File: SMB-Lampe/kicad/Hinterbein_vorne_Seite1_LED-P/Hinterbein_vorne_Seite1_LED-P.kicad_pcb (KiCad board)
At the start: 2 copper layers, 10.7 x 29.2 mm, 8 parts, among them J1 Conn_01x01_Pin, J2 Conn_01x01_Pin, J3 Conn_01x01_Pin

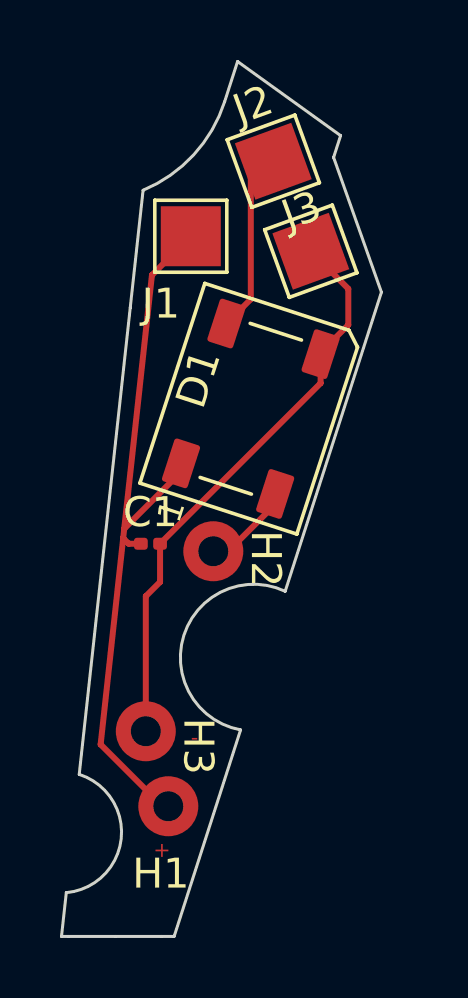
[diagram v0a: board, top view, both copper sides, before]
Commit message: Hinterbeine Geändert teilweiße Körper
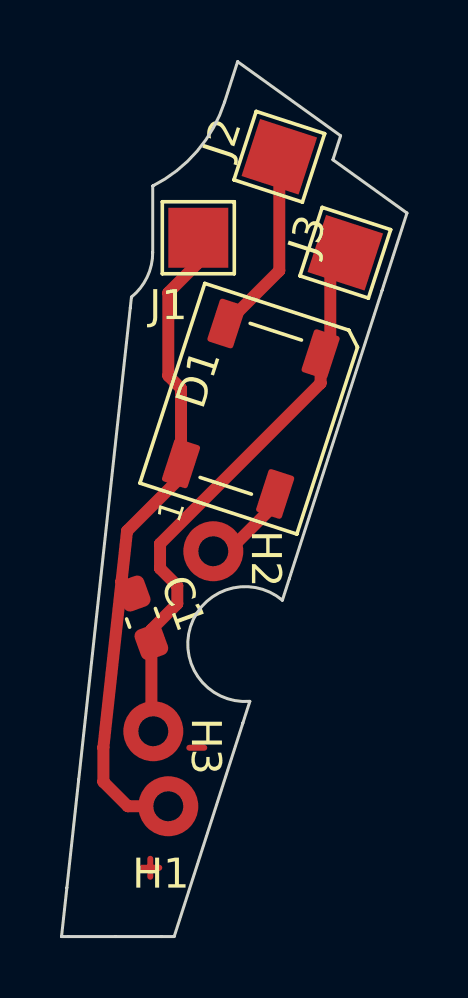
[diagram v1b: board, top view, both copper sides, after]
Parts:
- C1: footprint Capacitor_SMD:C_0201_0603Metric -> Capacitor_SMD:C_0603_1608Metric_Pad1.08x0.95mm_HandSolder
- moved C1 2.48 mm to (148.1, 78.5), turned to -70 degrees
- moved J3 1.15 mm to (154.9, 66.3), turned to 72 degrees
- moved J1 0.25 mm to (150.0, 65.8)
- moved H3 0.25 mm to (148.5, 82.2)
- moved J2 0.25 mm to (152.7, 63.1), turned to 72 degrees
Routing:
- net /Data_OUT_Hinterbein_vorne_Seite2: track 3.06 -> 5.61 mm
- net (no net): track 0.00 -> 1.70 mm
- net /+5V_IN_Körper_Seite2: track 24.0 -> 22.9 mm
- net /Data_IN_Körper_Seite2: track 6.33 -> 6.98 mm
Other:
- board size 10.7 x 29.2 mm -> 11.5 x 29.2 mm
- board text removed: "+"
- board text removed: "-"

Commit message: Alle Platinen sind fertig zur Fertigung
Aus diesem Stand folgt das erste fertig leuchtende Pferd
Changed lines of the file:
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@@
 		(tenting front back)
 		(pcbplotparams
-			(layerselection 0x00000000_00000000_55555555_57557573)
+			(layerselection 0x00000000_00000000_55555555_57555551)
 			(plot_on_all_layers_selection 0x00000000_00000000_00000000_00000000)
 			(disableapertmacros no)
@@
 	)
 	(gr_line
+		(start 149.9 63.9)
+		(end 149.9 64.5)
+		(stroke
+			(width 0.2)
+			(type default)
+		)
+		(layer "F.Cu")
+	)
+	(gr_line
+		(start 154.8 64.4)
+		(end 155.4 64.6)
+		(stroke
+			(width 0.2)
+			(type default)
+		)
+		(layer "F.Cu")
+	)
+	(gr_line
+		(start 155.2 68.4)
+		(end 155.2 68.5)
+		(stroke
+			(width 0.2)
+			(type default)
+		)
+		(layer "F.Cu")
+	)
+	(gr_line
+		(start 149.6 64.2)
+		(end 150.2 64.2)
+		(stroke
+			(width 0.2)
+			(type default)
+		)
+		(layer "F.Cu")
+	)
+	(gr_line

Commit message: Hauptplatine fertig
Hauptplatine mit ESP Levelshifter und Screwsockets
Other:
- board size 11.5 x 29.2 mm -> 617.2 x 280.6 mm
